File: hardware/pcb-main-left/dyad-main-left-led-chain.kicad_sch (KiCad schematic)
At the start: 64 parts

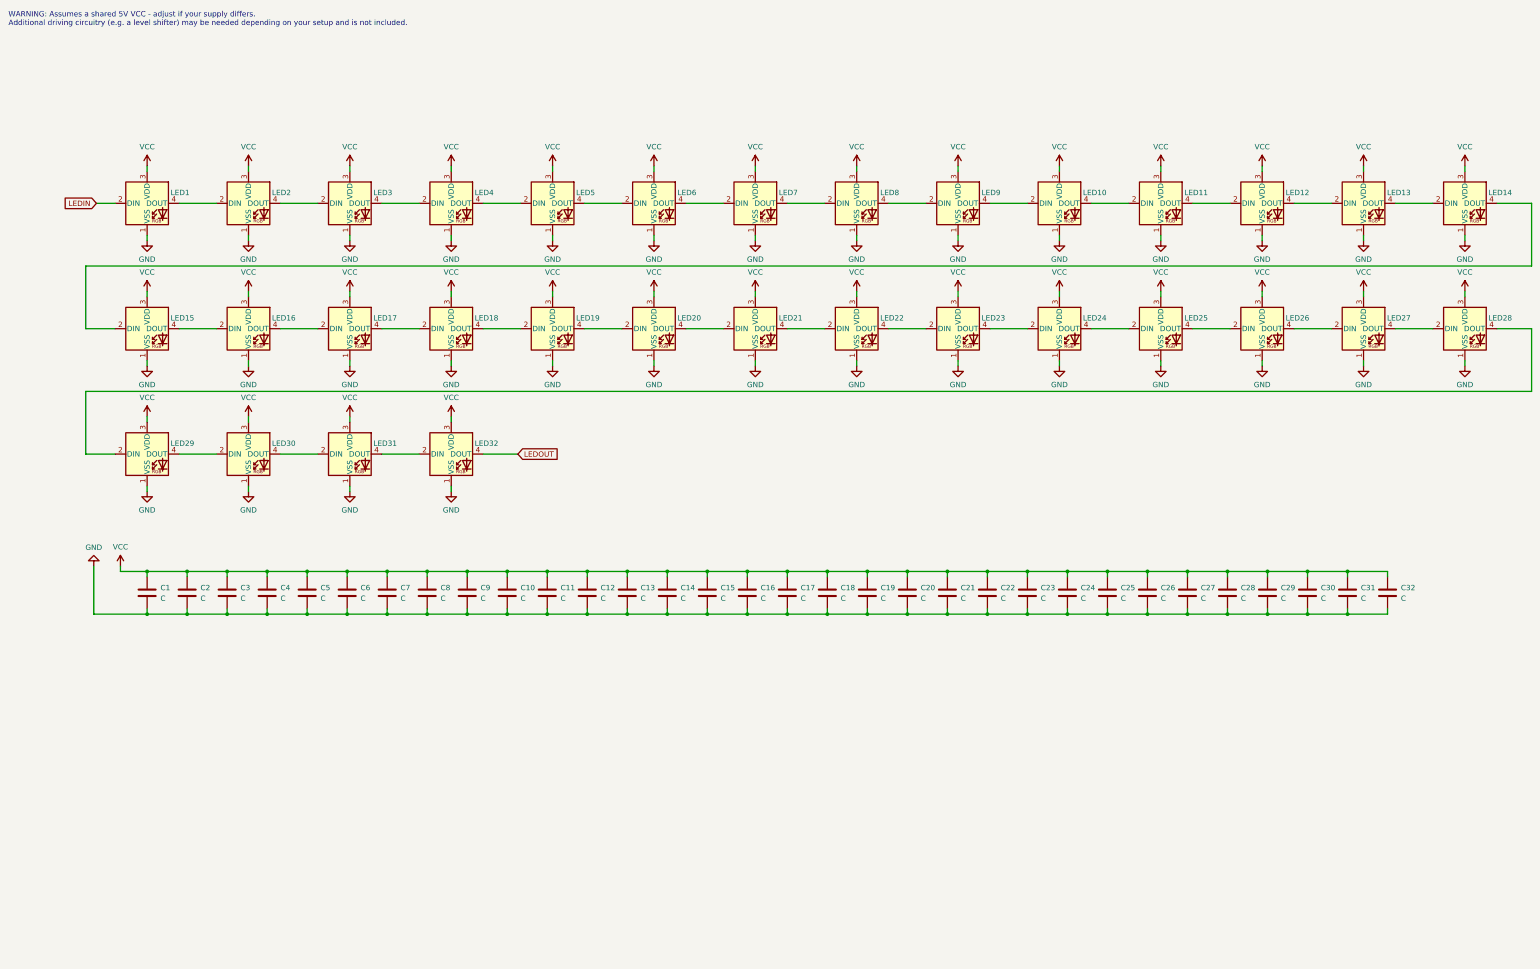
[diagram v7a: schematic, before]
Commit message: Left half fully routed, and repair a dragged board-outline corner
330 segments and 32 vias close every connection on main-left. Unconnected
125 -> 0, schematic parity 98 -> 0, no shorts.

Routing also caught a board-outline break that DRC reported as three
invalid_outline errors -- "Board has malformed outline (not a closed shape)".
Nothing was deleted: a three-segment rounded corner had been dragged by
exactly (-6.137, -4.900) mm, leaving a 2.85 mm gap where it belonged and a
dangling spur where it landed. Segment count stayed at 23 either way, which
is why it was not obvious; the tell was four Edge.Cuts endpoints used once
instead of zero.

Restored the three segments to their committed coordinates, then refilled
both pours -- they had been filled against the displaced edge and sat at
0.0000 mm from the restored one, which surfaced as two copper_edge_clearance
errors in between.

  invalid_outline        3 -> 0
  copper_edge_clearance  0 -> 2 -> 0
  Edge.Cuts open ends    4 -> 0

Both halves now carry only cosmetic silkscreen warnings and the deliberate
D/SW courtyard overlaps:

              violations  errors  unconnected  parity  shorts
  main-left          195      32            0       0       0
  main-right         253      37            0       0       0

Co-Authored-By: Claude Opus 5 <noreply@anthropic.com>
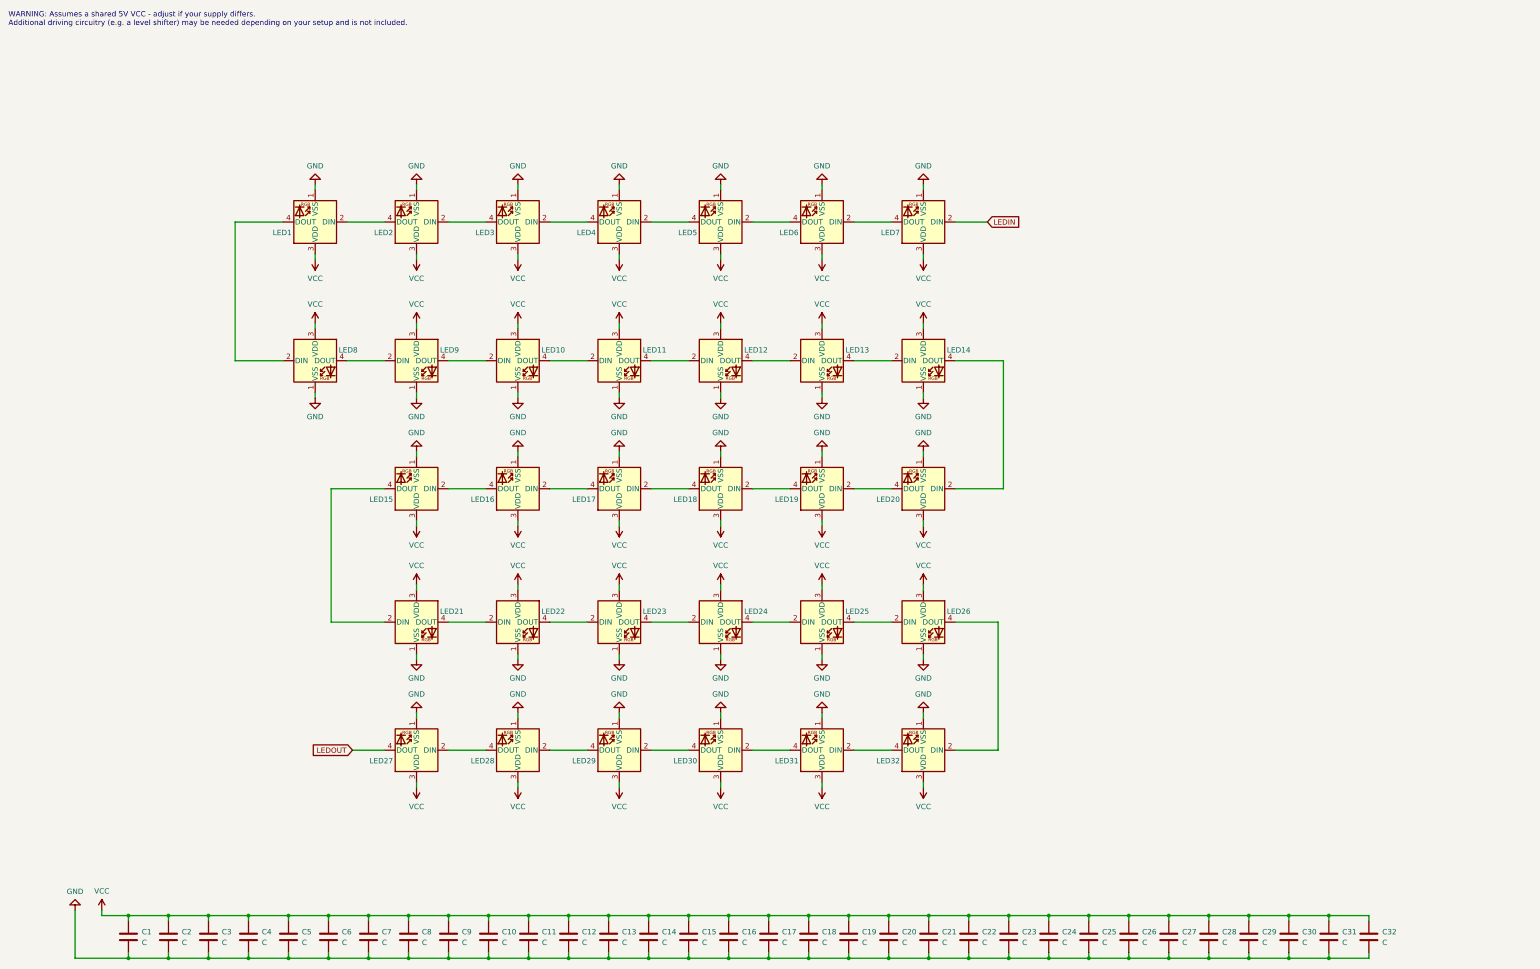
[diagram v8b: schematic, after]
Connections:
- net LEDIN: now also LED7.2 (DIN); no longer LED1.2 (DIN)
- net LEDOUT: now also LED27.4 (DOUT); no longer LED32.4 (DOUT)
- net at LED20.2 (DIN): now also LED14.4 (DOUT); no longer LED19.4 (DOUT)
- net at LED20.4 (DOUT): now also LED19.2 (DIN); no longer LED21.2 (DIN)
- net at LED5.2 (DIN): now also LED6.4 (DOUT); no longer LED4.4 (DOUT)
- net at LED5.4 (DOUT): now also LED4.2 (DIN); no longer LED6.2 (DIN)
- net at LED30.2 (DIN): now also LED31.4 (DOUT); no longer LED29.4 (DOUT)
- net at LED30.4 (DOUT): now also LED29.2 (DIN); no longer LED31.2 (DIN)
- net at LED28.4 (DOUT): now also LED27.2 (DIN); no longer LED29.2 (DIN)
- net at LED26.4 (DOUT): now also LED32.2 (DIN); no longer LED27.2 (DIN)
- net at LED15.2 (DIN): now also LED16.4 (DOUT); no longer LED14.4 (DOUT)
- net at LED15.4 (DOUT): now also LED21.2 (DIN); no longer LED16.2 (DIN)
- net at LED28.2 (DIN): now also LED29.4 (DOUT); no longer LED27.4 (DOUT)
- net at LED17.2 (DIN): now also LED18.4 (DOUT); no longer LED16.4 (DOUT)
- net at LED17.4 (DOUT): now also LED16.2 (DIN); no longer LED18.2 (DIN)
- net at LED1.4 (DOUT): now also LED8.2 (DIN); no longer LED2.2 (DIN)
- net at LED2.4 (DOUT): now also LED1.2 (DIN); no longer LED3.2 (DIN)
- net at LED7.4 (DOUT): now also LED6.2 (DIN); no longer LED8.2 (DIN)
- net at LED3.4 (DOUT): now also LED2.2 (DIN); no longer LED4.2 (DIN)
- new net: LED18.2 (DIN), LED19.4 (DOUT)
- new net: LED31.2 (DIN), LED32.4 (DOUT)
- new net: LED3.2 (DIN), LED4.4 (DOUT)
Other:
- moved on the sheet: C1, C10, C11, C12, C13, C14, C15, C16, C17, C18, C19, C2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
